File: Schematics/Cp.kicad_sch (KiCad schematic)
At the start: 64 parts, among them Q10 J201, Q11 J201, Q3 2SC1815, Q4 2SC1815, Q5 2SC1815, Q6 2SC1815, Q7 2SC1815, Q8 2SC1815, Q9 2SC1815, SW1 SW_Push, U1 CA3080

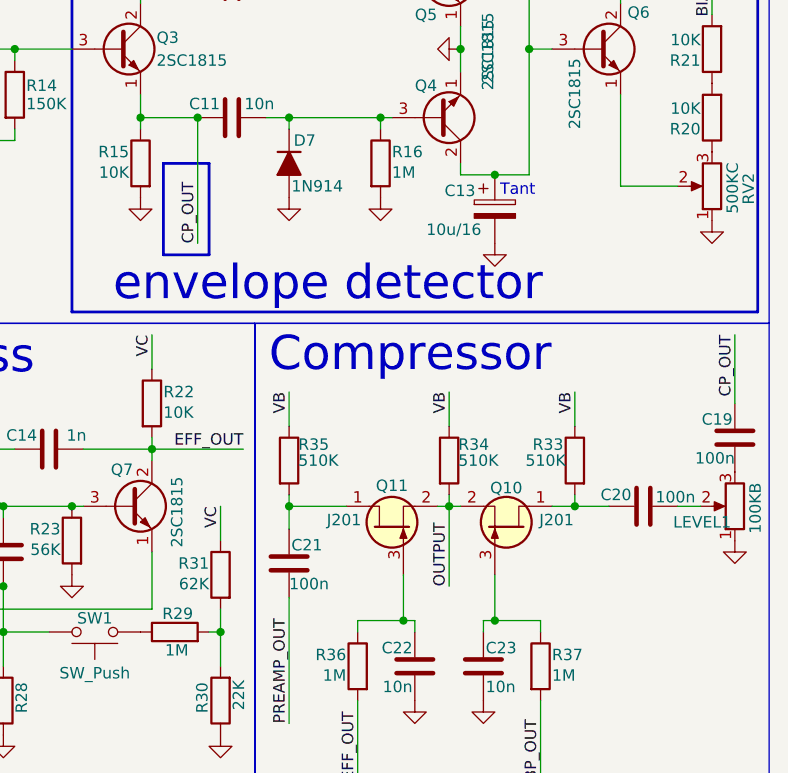
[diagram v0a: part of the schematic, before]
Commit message: Big upd
moved hierarical Sheets to direсtory Schematics, revorked power supply
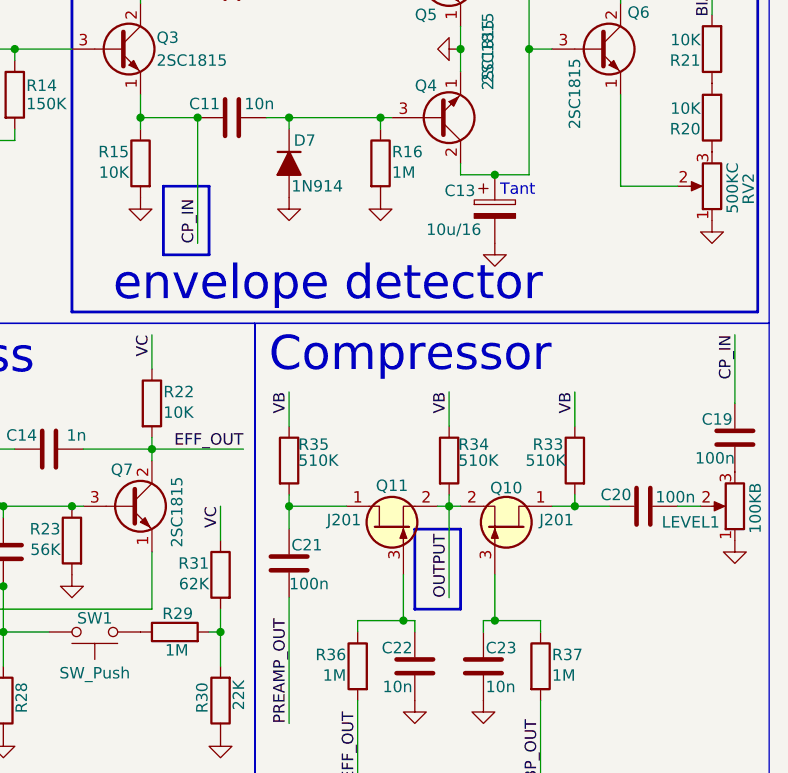
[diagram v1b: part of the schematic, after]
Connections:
- net CP_OUT renamed CP_IN
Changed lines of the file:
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@@
 	)
 	(rectangle
-		(start 99.06 50.8)
+		(start 127 91.44)
+		(end 132.08 100.33)
+		(radius 2.54)
+		(stroke
+			(width 0.3048)
+			(type solid)
+			(color 255 153 0 1)
+		)
+		(fill
+			(type none)
+		)
+	)
+	(rectangle
+		(start 99.06 53.34)
 		(end 104.14 60.96)
 		(radius 2.54)
@@
 	(wire
 		(pts
-			(xy 130.81 97.79) (xy 130.81 88.9)
+			(xy 130.81 99.06) (xy 130.81 88.9)
 		)
 		(stroke
@@
 		)
 	)
-	(label "CP_OUT"
+	(label "CP_IN"
 		(at 102.87 59.69 90)
 		(effects
@@
 		)
 	)
-	(label "CP_OUT"
+	(label "CP_IN"
 		(at 162.56 69.85 270)
 		(effects
@@
 	)
 	(label "OUTPUT"
-		(at 130.81 97.79 90)
+		(at 130.81 99.06 90)
 		(effects
 			(font
@@
 		(dnp no)
 		(property "Reference" "LEVEL1"
-			(at 155.702 90.678 0)
+			(at 154.432 90.678 0)
 			(show_name no)
 			(do_not_autoplace yes)

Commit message: footprints assigned
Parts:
- C10, C11, C12, C13, C14, C15, C16, C17, C18, C19, C20, C21, C22, C23, C7, C8, C9: footprint (none) -> Capacitor_THT:C_Disc_D7.0mm_W2.5mm_P5.00mm
- D3, D6, D7: footprint PCM_Diode_THT_AKL:D_DO-35_SOD27_P7.62mm_Horizontal -> Diode_THT:D_DO-35_SOD27_P7.62mm_Horizontal
- D5: footprint (none) -> LED_THT:LED_BL-FL7680RGB
- Q10, Q11: footprint PCM_Package_TO_SOT_THT_AKL:TO-92_Inline_Wide_DSG -> Package_TO_SOT_THT:TO-92_Inline
- R10, R11, R12, R13, R14, R15, R16, R17, R18, R19, R20, R21, R22, R23, R24, R25, R26, R27, R28, R29, R30, R31, R32, R33, R34, R35, R36, R37: footprint (none) -> Resistor_THT:R_Axial_DIN0207_L6.3mm_D2.5mm_P10.16mm_Horizontal
- RV1: footprint (none) -> Potentiometer_THT:Potentiometer_Vishay_248BH-249BH_Single_Horizontal
- SW1: footprint (none) -> Connector_PinSocket_2.54mm:PinSocket_1x02_P2.54mm_Horizontal
- U1: footprint Housing_DIP:DIP-8_W7.62mm -> Package_DIP:DIP-8_W7.62mm
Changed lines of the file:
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@@
 			)
 		)
-		(property "Footprint" ""
+		(property "Footprint" "Capacitor_THT:C_Disc_D7.0mm_W2.5mm_P5.00mm"
 			(at 77.1652 46.99 0)
 			(hide yes)
@@
 			)
 		)
-		(property "Footprint" ""
+		(property "Footprint" "Resistor_THT:R_Axial_DIN0207_L6.3mm_D2.5mm_P10.16mm_Horizontal"
 			(at 107.188 96.52 90)
 			(hide yes)
@@
 			)
 		)
-		(property "Footprint" ""
+		(property "Footprint" "Capacitor_THT:C_Disc_D7.0mm_W2.5mm_P5.00mm"
 			(at 156.21 87.9348 0)
 			(hide yes)
@@
 			)
 		)
-		(property "Footprint" ""
+		(property "Footprint" "Potentiometer_THT:Potentiometer_Vishay_248BH-249BH_Single_Horizontal"
 			(at 36.83 40.64 0)
 			(hide yes)
@@
 			)
 		)
-		(property "Footprint" ""
+		(property "Footprint" "Resistor_THT:R_Axial_DIN0207_L6.3mm_D2.5mm_P10.16mm_Horizontal"
 			(at 27.94 102.108 90)
 			(hide yes)
@@
 			)
 		)
-		(property "Footprint" ""
+		(property "Footprint" "Capacitor_THT:C_Disc_D7.0mm_W2.5mm_P5.00mm"
 			(at 51.1048 64.77 0)
 			(hide yes)
@@
 			)
 		)
-		(property "Footprint" ""
+		(property "Footprint" "Resistor_THT:R_Axial_DIN0207_L6.3mm_D2.5mm_P10.16mm_Horizontal"
 			(at 46.228 60.96 90)
 			(hide yes)
@@
 			)
 		)
-		(property "Footprint" ""
+		(property "Footprint" "Resistor_THT:R_Axial_DIN0207_L6.3mm_D2.5mm_P10.16mm_Horizontal"
 			(at 80.772 43.18 90)
 			(hide yes)
@@
 			)
 		)
-		(property "Footprint" ""
+		(property "Footprint" "Capacitor_THT:C_Disc_D7.0mm_W2.5mm_P5.00mm"
 			(at 110.49 44.7548 0)
 			(hide yes)
@@
 			)
 		)
-		(property "Footprint" ""
+		(property "Footprint" "Capacitor_THT:C_Disc_D7.0mm_W2.5mm_P5.00mm"
 			(at 72.39 81.5848 0)
 			(hide yes)
@@
 			)
 		)
-		(property "Footprint" ""
+		(property "Footprint" "Resistor_THT:R_Axial_DIN0207_L6.3mm_D2.5mm_P10.16mm_Horizontal"
 			(at 52.832 52.07 90)
 			(hide yes)
@@
 			)
 		)
-		(property "Footprint" ""
+		(property "Footprint" "Resistor_THT:R_Axial_DIN0207_L6.3mm_D2.5mm_P10.16mm_Horizontal"
 			(at 96.012 77.47 90)
 			(hide yes)
@@
 			)
 		)
-		(property "Footprint" ""
+		(property "Footprint" "Resistor_THT:R_Axial_DIN0207_L6.3mm_D2.5mm_P10.16mm_Horizontal"
 			(at 144.78 25.908 90)
 			(hide yes)
@@
 			)
 		)
-		(property "Footprint" ""
+		(property "Footprint" "Connector_PinSocket_2.54mm:PinSocket_1x02_P2.54mm_Horizontal"
 			(at 91.44 107.95 0)
 			(hide yes)
@@
 			)
 		)
-		(property "Footprint" ""
+		(property "Footprint" "Resistor_THT:R_Axial_DIN0207_L6.3mm_D2.5mm_P10.16mm_Horizontal"
 			(at 62.992 92.71 90)
 			(hide yes)
@@
 			)
 		)
-		(property "Footprint" ""
+		(property "Footprint" "Capacitor_THT:C_Disc_D7.0mm_W2.5mm_P5.00mm"
 			(at 90.17 81.5848 0)
 			(hide yes)
@@
 			)
 		)
-		(property "Footprint" ""
+		(property "Footprint" "Capacitor_THT:C_Disc_D7.0mm_W2.5mm_P5.00mm"
 			(at 127.9652 102.87 0)
 			(hide yes)
@@
 			)
 		)
-		(property "Footprint" ""
+		(property "Footprint" "Resistor_THT:R_Axial_DIN0207_L6.3mm_D2.5mm_P10.16mm_Horizontal"
 			(at 30.988 60.96 90)
 			(hide yes)
@@
 			)
 		)
-		(property "Footprint" ""
+		(property "Footprint" "Resistor_THT:R_Axial_DIN0207_L6.3mm_D2.5mm_P10.16mm_Horizontal"
 			(at 120.142 25.4 90)
 			(hide yes)
@@
 			)
 		)
-		(property "Footprint" ""
+		(property "Footprint" "Capacitor_THT:C_Disc_D7.0mm_W2.5mm_P5.00mm"
 			(at 110.49 29.5148 0)
 			(hide yes)
@@
 			)
 		)
-		(property "Footprint" ""
+		(property "Footprint" "Capacitor_THT:C_Disc_D7.0mm_W2.5mm_P5.00mm"
 			(at 48.5648 55.88 0)
 			(hide yes)
@@
 			)
 		)
-		(property "Footprint" ""
+		(property "Footprint" "LED_THT:LED_BL-FL7680RGB"
 			(at 24.13 87.63 0)
 			(hide yes)
@@
 			)
 		)
-		(property "Footprint" "PCM_Diode_THT_AKL:D_DO-35_SOD27_P7.62mm_Horizontal"
+		(property "Footprint" "Diode_THT:D_DO-35_SOD27_P7.62mm_Horizontal"
 			(at 35.56 100.33 0)
 			(hide yes)
@@
 			)
 		)
-		(property "Footprint" ""
+		(property "Footprint" "Capacitor_THT:C_Disc_D7.0mm_W2.5mm_P5.00mm"
 			(at 112.0648 91.44 0)
 			(hide yes)
@@
 			)
 		)
-		(property "Footprint" ""
+		(property "Footprint" "Resistor_THT:R_Axial_DIN0207_L6.3mm_D2.5mm_P10.16mm_Horizontal"
 			(at 129.032 83.82 90)
 			(hide yes)
@@
 			)
 		)
-		(property "Footprint" ""
+		(property "Footprint" "Capacitor_THT:C_Disc_D7.0mm_W2.5mm_P5.00mm"
 			(at 70.1548 46.99 0)
 			(hide yes)
@@
 			)
 		)
-		(property "Footprint" ""
+		(property "Footprint" "Resistor_THT:R_Axial_DIN0207_L6.3mm_D2.5mm_P10.16mm_Horizontal"
 			(at 54.102 77.47 90)
 			(hide yes)
@@
 			)
 		)
-		(property "Footprint" ""
+		(property "Footprint" "Resistor_THT:R_Axial_DIN0207_L6.3mm_D2.5mm_P10.16mm_Horizontal"
 			(at 22.352 78.74 90)
 			(hide yes)
@@
 			)
 		)
-		(property "Footprint" "Housing_DIP:DIP-8_W7.62mm"
+		(property "Footprint" "Package_DIP:DIP-8_W7.62mm"
 			(at 62.23 38.1 0)
 			(hide yes)
@@
 			)
 		)
-		(property "Footprint" ""
+		(property "Footprint" "Resistor_THT:R_Axial_DIN0207_L6.3mm_D2.5mm_P10.16mm_Horizontal"
 			(at 146.558 83.82 90)
 			(hide yes)
@@
 			)
 		)
-		(property "Footprint" ""
+		(property "Footprint" "Capacitor_THT:C_Disc_D7.0mm_W2.5mm_P5.00mm"
 			(at 82.2452 90.17 0)
 			(hide yes)
@@
 			)
 		)
-		(property "Footprint" ""
+		(property "Footprint" "Resistor_THT:R_Axial_DIN0207_L6.3mm_D2.5mm_P10.16mm_Horizontal"
 			(at 94.742 25.4 90)
 			(hide yes)
@@
 			)
 		)
-		(property "Footprint" ""
+		(property "Footprint" "Capacitor_THT:C_Disc_D7.0mm_W2.5mm_P5.00mm"
 			(at 163.5252 77.47 0)
 			(hide yes)
@@
 			)
 		)
-		(property "Footprint" ""
+		(property "Footprint" "Capacitor_THT:C_Disc_D7.0mm_W2.5mm_P5.00mm"
 			(at 71.4248 90.17 0)
 			(hide yes)
@@
 			)
 		)
-		(property "Footprint" ""
+		(property "Footprint" "Resistor_THT:R_Axial_DIN0207_L6.3mm_D2.5mm_P10.16mm_Horizontal"
 			(at 38.608 60.96 90)
 			(hide yes)
@@
 			)
 		)
-		(property "Footprint" ""
+		(property "Footprint" "Resistor_THT:R_Axial_DIN0207_L6.3mm_D2.5mm_P10.16mm_Horizontal"
 			(at 90.678 92.71 90)
 			(hide yes)
@@
 			)
 		)
-		(property "Footprint" ""
+		(property "Footprint" "Resistor_THT:R_Axial_DIN0207_L6.3mm_D2.5mm_P10.16mm_Horizontal"
 			(at 107.188 110.49 90)
 			(hide yes)
@@
 			)
 		)
-		(property "Footprint" "PCM_Package_TO_SOT_THT_AKL:TO-92_Inline_Wide_DSG"
+		(property "Footprint" "Package_TO_SOT_THT:TO-92_Inline"
 			(at 121.92 86.36 0)
 			(hide yes)
@@
 			)
 		)
-		(property "Footprint" ""
+		(property "Footprint" "Resistor_THT:R_Axial_DIN0207_L6.3mm_D2.5mm_P10.16mm_Horizontal"
 			(at 100.33 104.648 90)
 			(hide yes)
@@
 			)
 		)
-		(property "Footprint" "PCM_Package_TO_SOT_THT_AKL:TO-92_Inline_Wide_DSG"
+		(property "Footprint" "Package_TO_SOT_THT:TO-92_Inline"
 			(at 139.7 86.36 0)
 			(hide yes)
@@
 			)
 		)
-		(property "Footprint" ""
+		(property "Footprint" "Resistor_THT:R_Axial_DIN0207_L6.3mm_D2.5mm_P10.16mm_Horizontal"
 			(at 139.192 106.68 90)
 			(hide yes)
@@
 			)
 		)
-		(property "Footprint" ""
+		(property "Footprint" "Resistor_THT:R_Axial_DIN0207_L6.3mm_D2.5mm_P10.16mm_Horizontal"
 			(at 121.412 50.8 90)
 			(hide yes)
@@
 			)
 		)
-		(property "Footprint" ""
+		(property "Footprint" "Resistor_THT:R_Axial_DIN0207_L6.3mm_D2.5mm_P10.16mm_Horizontal"
 			(at 79.502 110.49 90)
 			(hide yes)
@@
 			)
 		)
-		(property "Footprint" "PCM_Diode_THT_AKL:D_DO-35_SOD27_P7.62mm_Horizontal"
+		(property "Footprint" "Diode_THT:D_DO-35_SOD27_P7.62mm_Horizontal"
 			(at 113.03 50.8 0)
 			(hide yes)
@@
 			)
 		)
-		(property "Footprint" ""
+		(property "Footprint" "Resistor_THT:R_Axial_DIN0207_L6.3mm_D2.5mm_P10.16mm_Horizontal"
 			(at 98.298 50.8 90)
 			(hide yes)
@@
 			)
 		)
-		(property "Footprint" "PCM_Diode_THT_AKL:D_DO-35_SOD27_P7.62mm_Horizontal"
+		(property "Footprint" "Diode_THT:D_DO-35_SOD27_P7.62mm_Horizontal"
 			(at 113.03 25.4 0)
 			(hide yes)
@@
 			)
 		)
-		(property "Footprint" ""
+		(property "Footprint" "Capacitor_THT:C_Disc_D7.0mm_W2.5mm_P5.00mm"
 			(at 136.8552 59.69 0)
 			(hide yes)
@@
 			)
 		)
-		(property "Footprint" ""
+		(property "Footprint" "Capacitor_THT:C_Disc_D7.0mm_W2.5mm_P5.00mm"
 			(at 71.12 108.2548 0)
 			(hide yes)
@@
 			)
 		)
-		(property "Footprint" ""
+		(property "Footprint" "Resistor_THT:R_Axial_DIN0207_L6.3mm_D2.5mm_P10.16mm_Horizontal"
 			(at 111.252 83.82 90)
 			(hide yes)
@@
 			)
 		)
-		(property "Footprint" ""
+		(property "Footprint" "Resistor_THT:R_Axial_DIN0207_L6.3mm_D2.5mm_P10.16mm_Horizontal"
 			(at 122.428 106.68 90)
 			(hide yes)
@@
 			)
 		)
-		(property "Footprint" ""
+		(property "Footprint" "Resistor_THT:R_Axial_DIN0207_L6.3mm_D2.5mm_P10.16mm_Horizontal"
 			(at 161.798 45.72 90)
 			(hide yes)
@@
 			)
 		)
-		(property "Footprint" ""
+		(property "Footprint" "Capacitor_THT:C_Disc_D7.0mm_W2.5mm_P5.00mm"
 			(at 133.6548 102.87 0)
 			(hide yes)
@@
 			)
 		)
-		(property "Footprint" ""
+		(property "Footprint" "Resistor_THT:R_Axial_DIN0207_L6.3mm_D2.5mm_P10.16mm_Horizontal"
 			(at 161.798 38.1 90)
 			(hide yes)
@@
 			)
 		)
-		(property "Footprint" ""
+		(property "Footprint" "Resistor_THT:R_Axial_DIN0207_L6.3mm_D2.5mm_P10.16mm_Horizontal"
 			(at 50.8 84.328 90)
 			(hide yes)

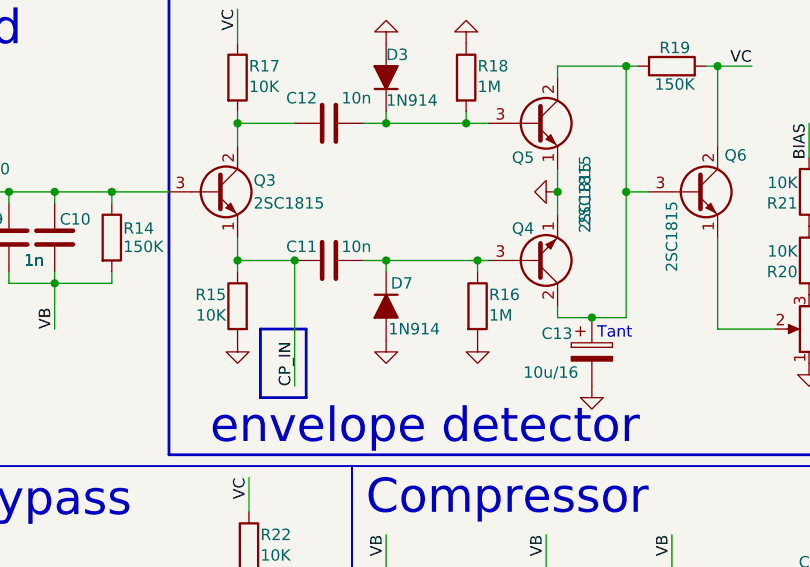
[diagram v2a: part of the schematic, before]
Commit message: directory cleared, Schem upd
The input mixer changed from passive to active(TL072)
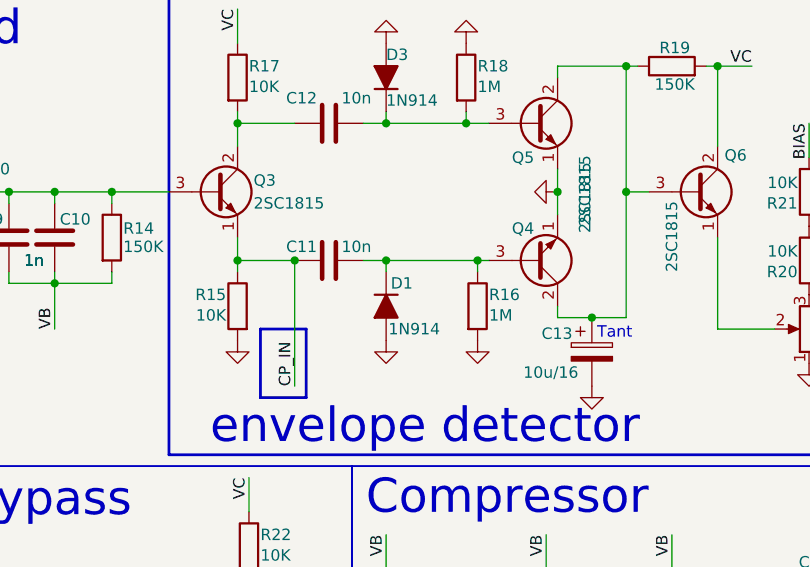
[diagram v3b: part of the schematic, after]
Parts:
- renumbered D7 to D1
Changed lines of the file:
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@@
 		(in_pos_files yes)
 		(dnp no)
-		(property "Reference" "D7"
+		(property "Reference" "D1"
 			(at 113.538 48.26 90)
 			(show_name no)
@@
 			(project "AMP-MA"
 				(path "/4094031b-a9da-4ac5-aaa1-42b342c92a3e/d432553b-ab0c-45ec-bbdd-5af2e9267855"
-					(reference "D7")
+					(reference "D1")
 					(unit 1)
 				)

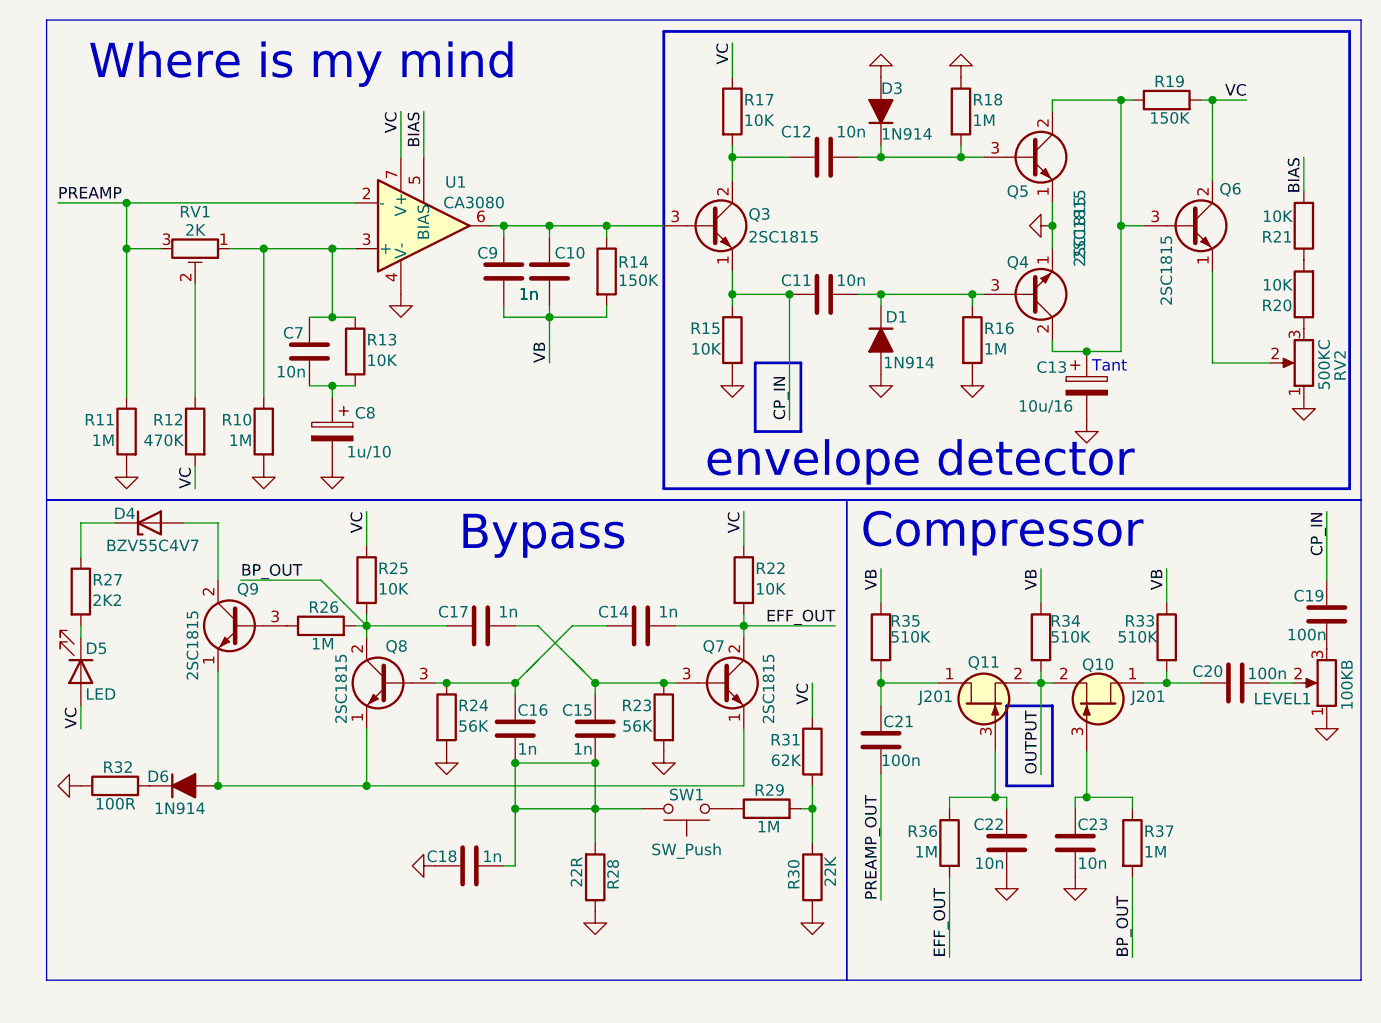
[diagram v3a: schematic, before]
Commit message: Schem upd
in bypass button changed on SPDT switch
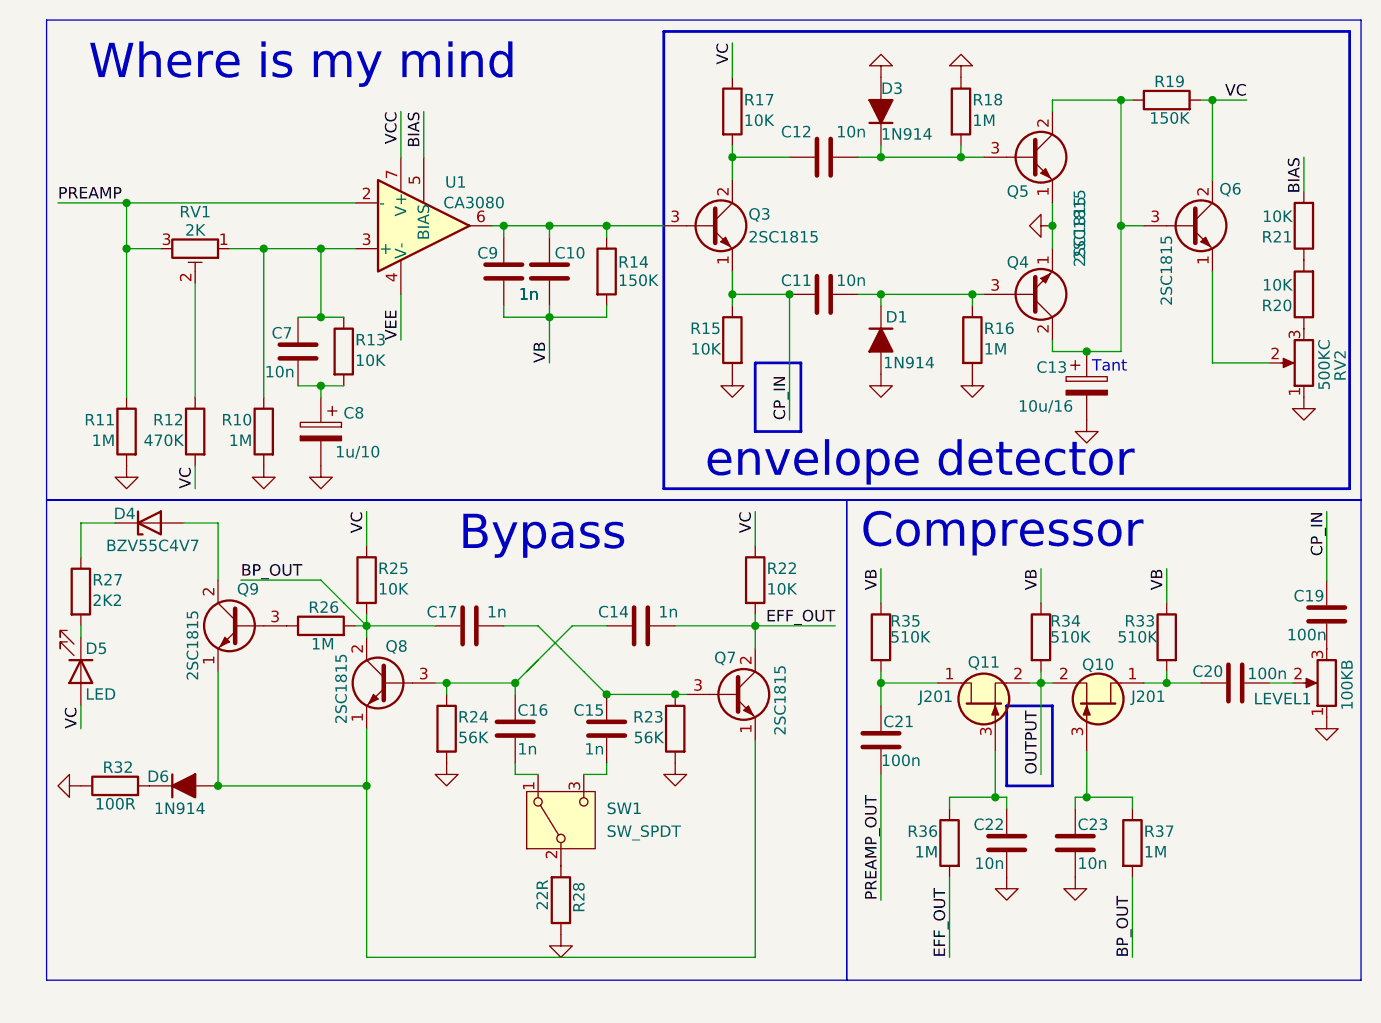
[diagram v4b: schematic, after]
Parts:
- removed C18: 1n, Capacitor_THT:C_Disc_D7.0mm_W2.5mm_P5.00mm, symbol Device:C
- removed R29: 1M, Resistor_THT:R_Axial_DIN0207_L6.3mm_D2.5mm_P10.16mm_Horizontal, symbol Device:R
- removed R30: 22K, Resistor_THT:R_Axial_DIN0207_L6.3mm_D2.5mm_P10.16mm_Horizontal, symbol Device:R
- removed R31: 62K, Resistor_THT:R_Axial_DIN0207_L6.3mm_D2.5mm_P10.16mm_Horizontal, symbol Device:R
- removed SW1: SW_Push, Connector_PinSocket_2.54mm:PinSocket_1x02_P2.54mm_Horizontal, symbol Switch:SW_Push
- added SW1: SW_SPDT, Button_Switch_SMD:SW_SPDT_CK_JS102011SAQN, symbol Switch:SW_SPDT
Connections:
- net GND: no longer U1.4 (V-)
- net VC: no longer U1.7 (V+)
- new net: C15.1, SW1.3 (C)
- new net: C16.1, SW1.1 (A)
- new net: R28.2, SW1.2 (B)
- new net VCC: U1.7 (V+)
- new net VEE: U1.4 (V-)
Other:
- moved on the sheet: C15, C17, C7, C8, Q7, R13, R22, R23, R24, R28
